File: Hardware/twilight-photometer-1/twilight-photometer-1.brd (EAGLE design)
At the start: 49.5 x 40.6 mm, 9 parts, among them U1 TLC271BIDR

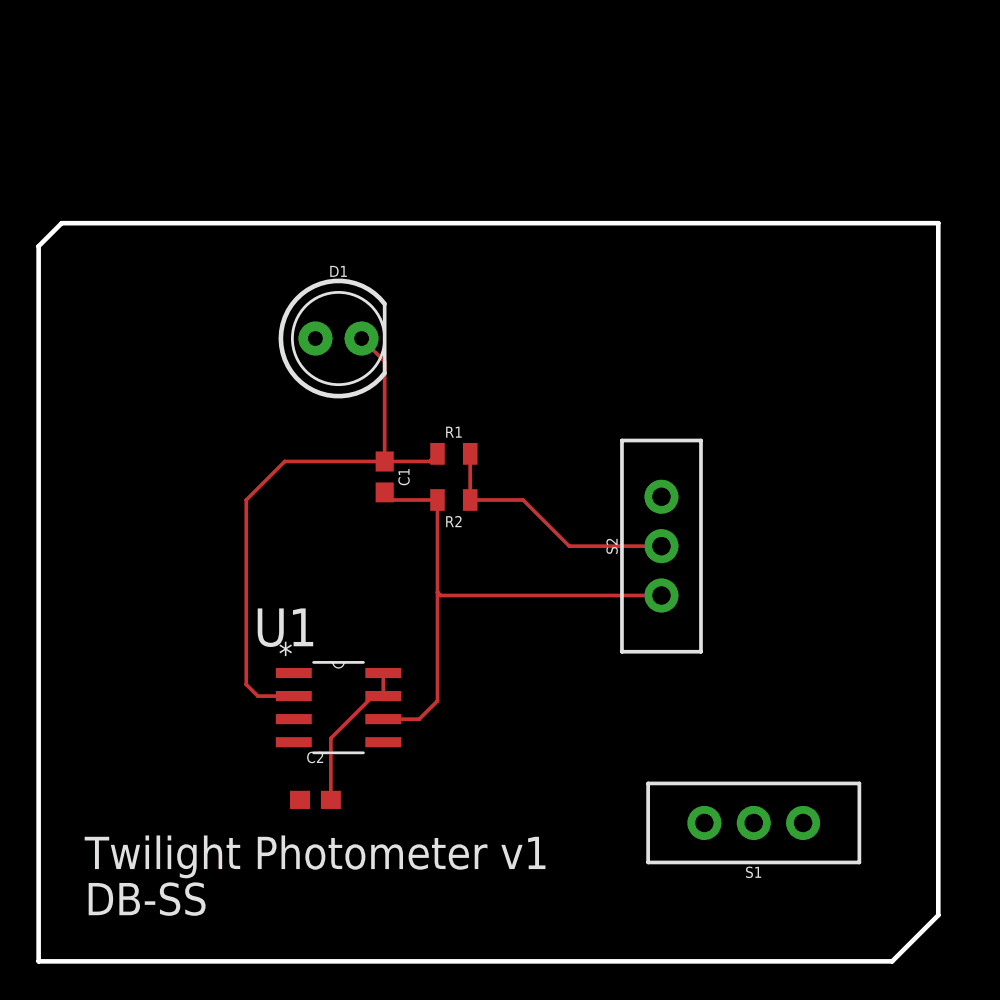
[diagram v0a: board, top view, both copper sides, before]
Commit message: Finished routing, Board sizing for V1
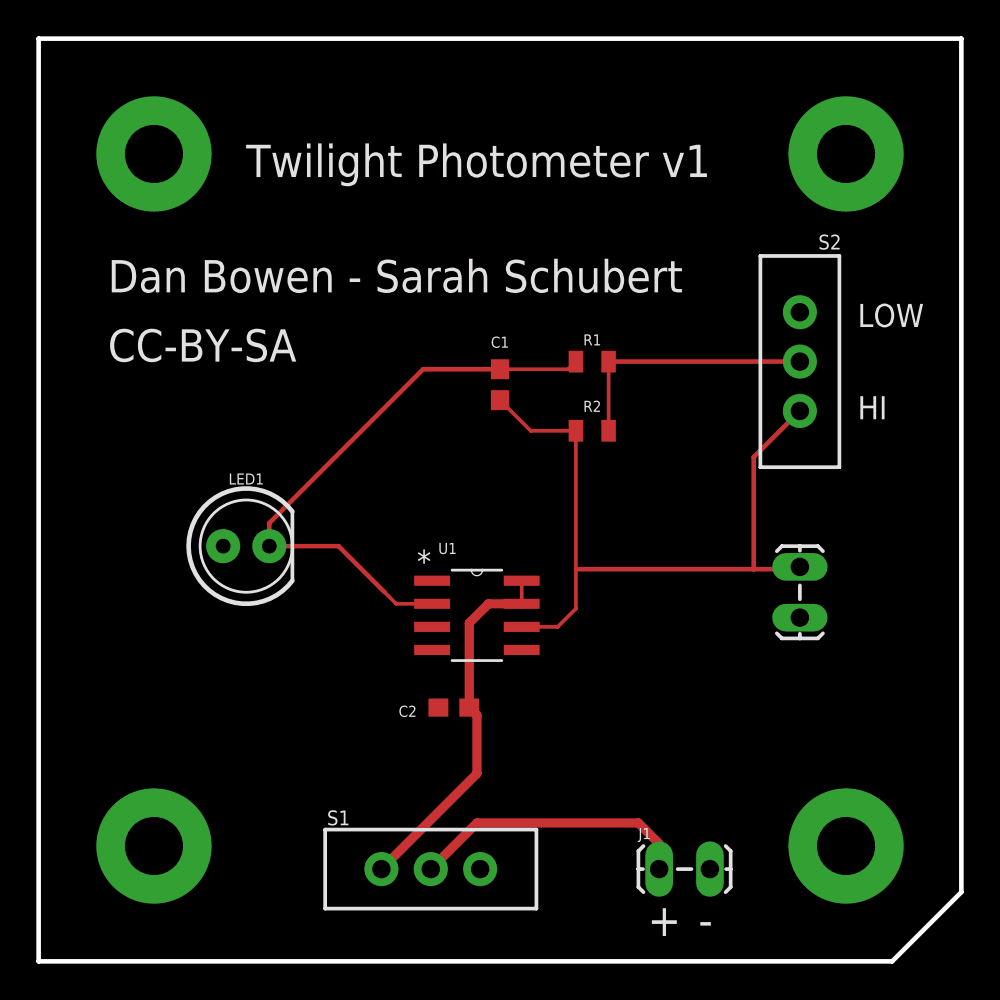
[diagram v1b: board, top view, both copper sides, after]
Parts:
- removed D1: (no value), SparkFun-LED:LED_5MM
- removed FRAME1: FRAME-LETTER, SparkFun-Aesthetics:CREATIVE_COMMONS
- added H1, H2, H3, H4: STANDOFF_ELECTRICAL, SparkFun-Hardware:STANDOFF-ELECTRICAL
- added J1: BATT IN, SparkFun-Connectors:1X02_LOCK_LONGPADS
- added J2: Signal Out, SparkFun-Connectors:1X02_LOCK_LONGPADS
- added LED1: (no value), SparkFun-LED:LED_5MM
- R1, R2: value (none) -> 50GΩ
- S1: value (none) -> ON - OFF
- S2: value (none) -> GAIN
- moved S1 18.0 mm to (21.6, 5.08), turned to 270 degrees
- moved S2 12.7 mm to (41.9, 33.0)
- moved R1 9.16 mm to (30.5, 33.0)
- moved C2 9.16 mm to (22.9, 14.0)
- moved U1 9.16 mm to (24.1, 19.1)
- moved R2 8.52 mm to (30.5, 29.2)
- moved C1 8.13 mm to (25.4, 31.8)
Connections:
- new net N$3: J1.1, S1.2
- net GND: now also H1.P1, H2.P1, H3.P1, H4.P1, J1.2, J2.2, LED1.A; no longer D1.A
- net N$2: now also LED1.K; no longer D1.K
- net N$5: now also J2.1
- net VDD: now also S1.3
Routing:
- net N$3: track 0.00 -> 15.5 mm
- net VDD: track 8.51 -> 20.5 mm
- net N$5: track 30.0 -> 40.2 mm
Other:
- board size 49.5 x 40.6 mm -> 50.8 x 50.8 mm
- board text added: "+"
- board text added: "-"
- board text added: "CC-BY-SA"
- board text added: "Dan Bowen - Sarah Schubert"
- board text added: "HI"
- board text added: "LOW"
- board text added: "Orig Forrest Mims III"
- board text removed: "DB-SS"
